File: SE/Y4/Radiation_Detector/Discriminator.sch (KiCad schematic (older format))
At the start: 17 parts, among them U12 SN74LVC1G74, U13 TS3011, U14 74AUP1G04

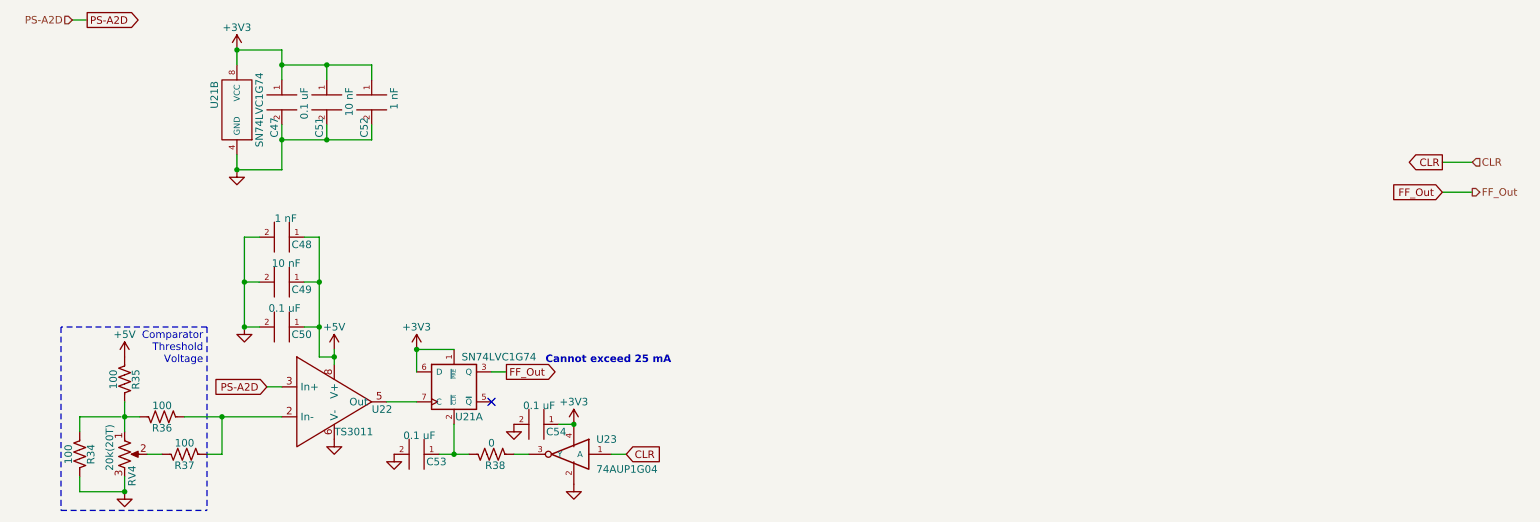
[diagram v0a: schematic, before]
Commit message: updated schematic labeling
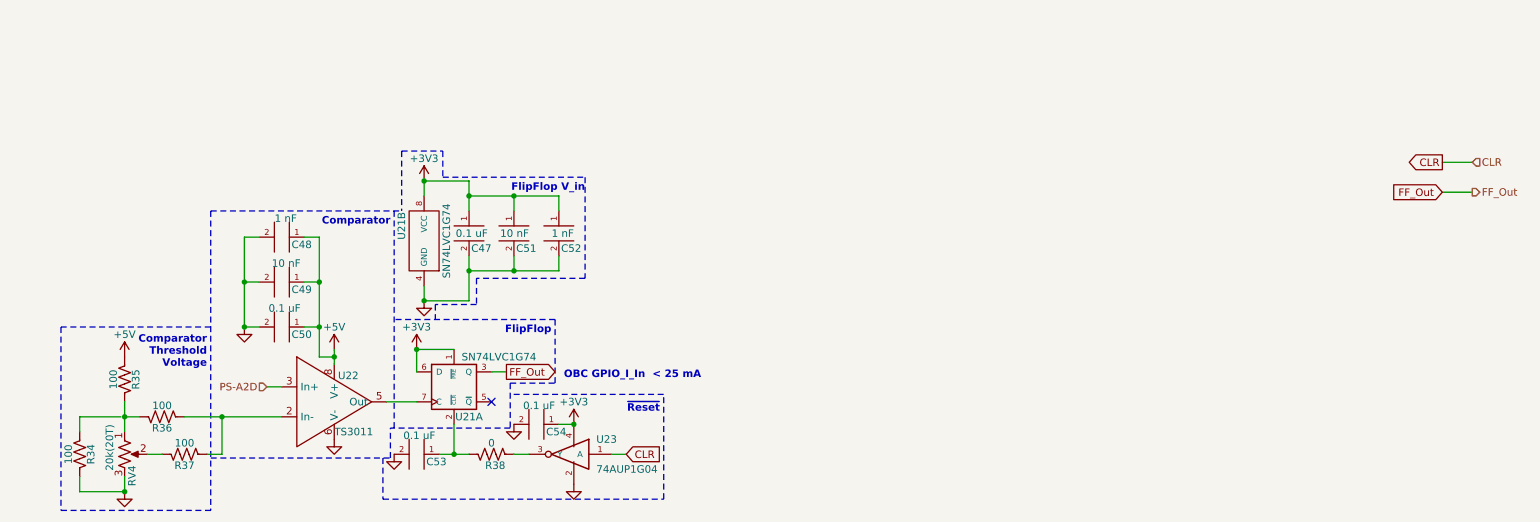
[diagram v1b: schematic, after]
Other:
- note added: "Comparator"
- note added: "FlipFlop"
- note added: "FlipFlop V_in\n"
- note added: "OBC GPIO_I_In < 25 mA\n"
- note added: "~Reset"
- note removed: "Cannot exceed 25 mA\n"
- moved on the sheet: C47, C51, C52, U21B
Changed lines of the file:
@@
 Wire Wire Line
 	1450 3450 1350 3450
-Text GLabel 2150 3000 0    50   Input ~ 0
-PS-A2D
 $Comp
 L Device:R_US R?
@@
 	1    0    0    1
 $EndComp
-Text HLabel 850  550  0    50   Input ~ 0
-PS-A2D
-Text GLabel 950  550  2    50   Output ~ 0
+Text HLabel 2150 3000 0    50   Input ~ 0
 PS-A2D
 Wire Wire Line
@@
 AR Path="/5EEC8340/5F1D2F6C/5EEEB1B9" Ref="U64"  Part="1"
 AR Path="/5EECD93E/5F1D2F6C/5EEEB1B9" Ref="U79"  Part="1"
-F 0 "U22" H 2850 2450 50  0000 L CNN
+F 0 "U22" H 2625 2675 50  0000 L CNN
 F 1 "TS3011" H 2600 2300 50  0000 L CNN
 F 2 "" H 1950 3000 50  0001 C CNN
@@
 L SS:SN74LVC1G74 U?
 U 2 1 5EF6BDB6
-P 2050 1350
+P 3300 2225
 AR Path="/5EBDE6C5/5EED755D/5EF6BDB6" Ref="U?"  Part="2"
 AR Path="/5EBDE6C5/5EFEC695/5EF6BDB6" Ref="U?"  Part="2"
@@
 AR Path="/5EEC8340/5F1D2F6C/5EF6BDB6" Ref="U63"  Part="2"
 AR Path="/5EECD93E/5F1D2F6C/5EF6BDB6" Ref="U78"  Part="2"
-F 0 "U21" H 2350 1100 50  0000 C CNN
-F 1 "SN74LVC1G74" H 2250 1400 50  0000 C CNN
-F 2 "" H 1500 1400 50  0001 C CNN
-F 3 "" H 1500 1400 50  0001 C CNN
-	2    2050 1350
+F 0 "U21" H 3600 1975 50  0000 C CNN
+F 1 "SN74LVC1G74" H 3500 2275 50  0000 C CNN
+F 2 "" H 2750 2275 50  0001 C CNN
+F 3 "" H 2750 2275 50  0001 C CNN
+	2    3300 2225
 	0    1    -1   0
 $EndComp
@@
 L 001:C C?
 U 1 1 5EF73564
-P 2250 950
+P 3500 1825
 AR Path="/5EF73564" Ref="C?"  Part="1"
 AR Path="/5EBDE6C5/5EF73564" Ref="C?"  Part="1"
@@
 AR Path="/5EEC8340/5F1D2F6C/5EF73564" Ref="C152"  Part="1"
 AR Path="/5EECD93E/5F1D2F6C/5EF73564" Ref="C189"  Part="1"
-F 0 "C47" H 2500 1000 50  0000 L CNN
-F 1 "0.1 uF" H 2300 800 50  0000 L CNN
-F 2 "" H 2300 1040 50  0001 C CNN
-F 3 "" H 2300 1040 50  0001 C CNN
-	1    2250 950
+F 0 "C47" V 3750 1675 50  0000 L CNN
+F 1 "0.1 uF" V 3650 1700 50  0000 L CNN
+F 2 "" H 3550 1915 50  0001 C CNN
+F 3 "" H 3550 1915 50  0001 C CNN
+	1    3500 1825
 	0    -1   1    0
 $EndComp
@@
 L 001:C C?
 U 1 1 5EF7356E
-P 2550 950
+P 3800 1825
 AR Path="/5EF7356E" Ref="C?"  Part="1"
 AR Path="/5EBDE6C5/5EF7356E" Ref="C?"  Part="1"
@@
 AR Path="/5EEC8340/5F1D2F6C/5EF7356E" Ref="C156"  Part="1"
 AR Path="/5EECD93E/5F1D2F6C/5EF7356E" Ref="C193"  Part="1"
-F 0 "C51" H 2800 1000 50  0000 L CNN
-F 1 "10 nF" H 2600 800 50  0000 L CNN
-F 2 "" H 2600 1040 50  0001 C CNN
-F 3 "" H 2600 1040 50  0001 C CNN
-	1    2550 950
+F 0 "C51" V 4050 1675 50  0000 L CNN
+F 1 "10 nF" V 3950 1725 50  0000 L CNN
+F 2 "" H 3850 1915 50  0001 C CNN
+F 3 "" H 3850 1915 50  0001 C CNN
+	1    3800 1825
 	0    -1   1    0
 $EndComp
@@
 L 001:C C?
 U 1 1 5EF73575
-P 2850 950
+P 4100 1825
 AR Path="/5EF73575" Ref="C?"  Part="1"
 AR Path="/5EBDE6C5/5EF73575" Ref="C?"  Part="1"
@@
 AR Path="/5EEC8340/5F1D2F6C/5EF73575" Ref="C157"  Part="1"
 AR Path="/5EECD93E/5F1D2F6C/5EF73575" Ref="C194"  Part="1"
-F 0 "C52" H 3100 1000 50  0000 L CNN
-F 1 "1 nF" H 2900 800 50  0000 L CNN
-F 2 "" H 2900 1040 50  0001 C CNN
-F 3 "" H 2900 1040 50  0001 C CNN
-	1    2850 950
+F 0 "C52" V 4350 1675 50  0000 L CNN
+F 1 "1 nF" V 4250 1725 50  0000 L CNN
+F 2 "" H 4150 1915 50  0001 C CNN
+F 3 "" H 4150 1915 50  0001 C CNN
+	1    4100 1825
 	0    -1   1    0
 $EndComp
 Wire Wire Line
-	2250 850  2550 850
-Wire Wire Line
-	2550 850  2550 950
-Wire Wire Line
-	2850 850  2850 950
-Wire Wire Line
-	2850 1350 2850 1250
-Wire Wire Line
-	2550 1250 2550 1350
-Wire Wire Line
-	2250 850  2250 950
-Wire Wire Line
-	2250 850  2250 750
-Wire Wire Line
-	1950 750  1950 850
-Wire Wire Line
-	1950 1550 1950 1450
-Wire Wire Line
-	2250 1250 2250 1350
-Connection ~ 2250 1350
-Wire Wire Line
-	2250 1350 2250 1550
-Connection ~ 2550 1350
-Wire Wire Line
-	2550 1350 2250 1350
-Wire Wire Line
-	2550 1350 2850 1350
-Connection ~ 2250 850
-Connection ~ 2550 850
-Wire Wire Line
-	2550 850  2850 850
-Wire Wire Line
-	1950 750  2250 750
-Wire Wire Line
-	1950 1550 2250 1550
+	3500 1725 3800 1725
+Wire Wire Line
+	3800 1725 3800 1825
+Wire Wire Line
+	4100 1725 4100 1825
+Wire Wire Line
+	4100 2225 4100 2125
+Wire Wire Line
+	3800 2125 3800 2225
+Wire Wire Line
+	3500 1725 3500 1825
+Wire Wire Line
+	3500 1725 3500 1625
+Wire Wire Line
+	3200 1625 3200 1725
+Wire Wire Line
+	3200 2425 3200 2325
+Wire Wire Line
+	3500 2125 3500 2225
+Connection ~ 3500 2225
+Wire Wire Line
+	3500 2225 3500 2425
+Connection ~ 3800 2225
+Wire Wire Line
+	3800 2225 3500 2225
+Wire Wire Line
+	3800 2225 4100 2225
+Connection ~ 3500 1725
+Connection ~ 3800 1725
+Wire Wire Line
+	3800 1725 4100 1725
+Wire Wire Line
+	3200 1625 3500 1625
+Wire Wire Line
+	3200 2425 3500 2425
 Connection ~ 1850 3200
 Wire Wire Line
@@
 	3400 3450 3400 3250
 Connection ~ 3400 3450
-Text Notes 4850 2850 2    50   ~ 10
-Cannot exceed 25 mA\n
+Text Notes 4050 2650 2    50   ~ 10
+FlipFlop
 Text GLabel 3750 2900 2    50   Output ~ 0
 FF_Out
@@
 L power:GND #PWR?
 U 1 1 5F25B4E8
-P 1950 1550
+P 3200 2425
 AR Path="/5EBDE6C5/5F25B4E8" Ref="#PWR?"  Part="1"
 AR Path="/5EBF5005/5F25B4E8" Ref="#PWR?"  Part="1"
@@
 AR Path="/5EEC8340/5F1D2F6C/5F25B4E8" Ref="#PWR?"  Part="1"
 AR Path="/5EECD93E/5F1D2F6C/5F25B4E8" Ref="#PWR?"  Part="1"
-F 0 "#PWR?" H 1950 1300 50  0001 C CNN
-F 1 "GND" H 2050 1450 50  0001 C CNN
-F 2 "" H 1950 1550 50  0001 C CNN
-F 3 "" H 1950 1550 50  0001 C CNN
-	1    1950 1550
+F 0 "#PWR?" H 3200 2175 50  0001 C CNN
+F 1 "GND" H 3300 2325 50  0001 C CNN
+F 2 "" H 3200 2425 50  0001 C CNN
+F 3 "" H 3200 2425 50  0001 C CNN
+	1    3200 2425
 	1    0    0    -1
 $EndComp
-Wire Wire Line
-	950  550  850  550
 $Comp
 L power:+5V #PWR?
@@
 L power:+3V3 #PWR?
 U 1 1 5F26549C
-P 1950 750
+P 3200 1625
 AR Path="/5EBDE6C5/5F26549C" Ref="#PWR?"  Part="1"
 AR Path="/5EBDE6C5/5EED755D/5F26549C" Ref="#PWR?"  Part="1"
@@
 AR Path="/5EEC8340/5F1D2F6C/5F26549C" Ref="#PWR?"  Part="1"
 AR Path="/5EECD93E/5F1D2F6C/5F26549C" Ref="#PWR?"  Part="1"
-F 0 "#PWR?" H 1950 600 50  0001 C CNN
-F 1 "+3V3" H 1950 900 50  0000 C CNN
-F 2 "" H 1950 750 50  0001 C CNN
-F 3 "" H 1950 750 50  0001 C CNN
-	1    1950 750
+F 0 "#PWR?" H 3200 1475 50  0001 C CNN
+F 1 "+3V3" H 3200 1775 50  0000 C CNN
+F 2 "" H 3200 1625 50  0001 C CNN
+F 3 "" H 3200 1625 50  0001 C CNN
+	1    3200 1625
 	1    0    0    -1
 $EndComp
-Connection ~ 1950 1550
-Connection ~ 1950 750
+Connection ~ 3200 2425
+Connection ~ 3200 1625
 Wire Wire Line
 	900  3200 1175 3200
@@
 $EndComp
 Wire Notes Line
-	1750 2600 775  2600
+	1775 2600 775  2600
 Wire Notes Line
 	775  2600 775  3825
 Wire Notes Line
-	775  3825 1750 3825
-Wire Notes Line
-	1750 2600 1750 3825
-Text Notes 1725 2850 2    50   ~ 0
+	775  3825 1775 3825
+Text Notes 1750 2875 2    50   ~ 10
 Comparator\nThreshold\nVoltage
+Text Notes 2975 1925 2    50   ~ 10
+Comparator
+Wire Notes Line
+	4800 3750 4800 3050
+Wire Notes Line
+	4800 3050 3775 3050
+Wire Notes Line
+	3775 3275 2975 3275
+Wire Notes Line
+	2925 3475 2925 3750
+Wire Notes Line
+	2925 3750 4800 3750
+Wire Notes Line
+	2975 3475 2975 3275
+Wire Notes Line
+	1775 3475 2975 3475
+Wire Notes Line
+	3000 3275 3000 1825
+Wire Notes Line
+	3775 2975 4075 2975
+Wire Notes Line
+	4075 2550 3000 2550
+Wire Notes Line
+	3775 2975 3775 3275
+Text Notes 5050 2950 2    50   ~ 10
+OBC GPIO_I_In  < 25 mA\n
+Wire Notes Line
+	4075 2550 4075 2975
+Text Notes 4775 3175 2    50   ~ 10
+~Reset
+Wire Notes Line
+	1775 1825 1775 3825
+Wire Notes Line
+	3050 1425 3050 1825
+Wire Notes Line
+	1775 1825 3050 1825
+Wire Notes Line
+	3325 1425 3325 1600
+Wire Notes Line
+	3325 1600 4275 1600
+Wire Notes Line
+	3050 1425 3325 1425
+Wire Notes Line
+	4275 2275 3550 2275
+Wire Notes Line
+	3550 2275 3550 2450
+Wire Notes Line
+	3550 2450 3275 2450
+Wire Notes Line
+	3275 2450 3275 2550
+Wire Notes Line
+	4275 1600 4275 2275
+Text Notes 4275 1700 2    50   ~ 10
+FlipFlop V_in\n
 $EndSCHEMATC
